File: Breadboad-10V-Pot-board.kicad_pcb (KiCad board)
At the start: 2 copper layers, 50 x 29 mm, 27 parts, among them P1 DIP14, P2 DIP14, U1 TL072-, U2 TL072-, U3 TL072-

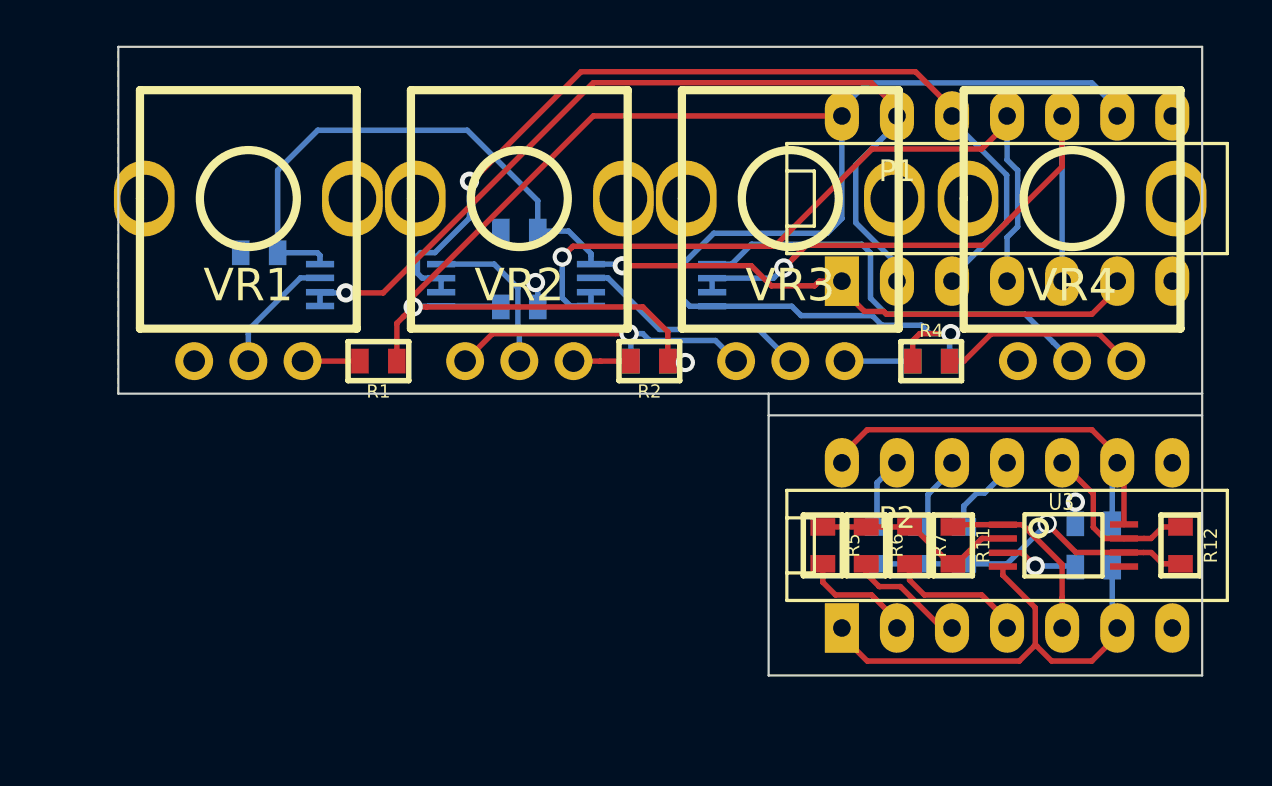
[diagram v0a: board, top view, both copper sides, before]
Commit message: added jack board and laid out mechanical holes for panel separation
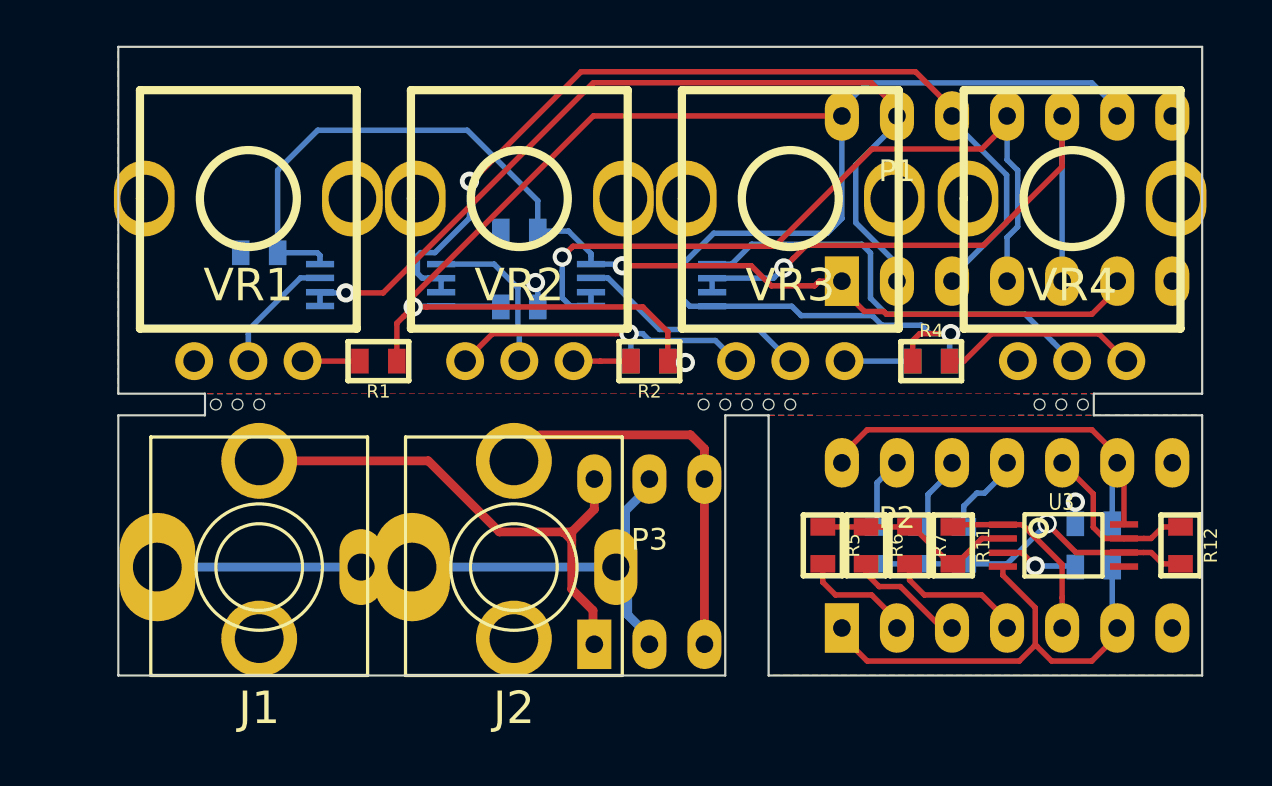
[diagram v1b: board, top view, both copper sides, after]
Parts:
- added HOLE-0.125-INCH: VAL**, MyModules:HOLE-0.125-INCH, F.Cu at (95.5, 48.5)
- added HOLE-0.125-INCH: VAL**, MyModules:HOLE-0.125-INCH, F.Cu at (120.0, 48.5)
- added HOLE-0.125-INCH: VAL**, MyModules:HOLE-0.125-INCH, F.Cu at (96.5, 48.5)
- added HOLE-0.125-INCH: VAL**, MyModules:HOLE-0.125-INCH, F.Cu at (107.8, 48.5)
- added HOLE-0.125-INCH: VAL**, MyModules:HOLE-0.125-INCH, F.Cu at (127.8, 48.5)
- added HOLE-0.125-INCH: VAL**, MyModules:HOLE-0.125-INCH, F.Cu at (97.5, 48.5)
- added HOLE-0.125-INCH: VAL**, MyModules:HOLE-0.125-INCH, F.Cu at (119.0, 48.5)
- added HOLE-0.125-INCH: VAL**, MyModules:HOLE-0.125-INCH, F.Cu at (118.0, 48.5)
- added HOLE-0.125-INCH: VAL**, MyModules:HOLE-0.125-INCH, F.Cu at (122.0, 48.5)
- added HOLE-0.125-INCH: VAL**, MyModules:HOLE-0.125-INCH, F.Cu at (133.5, 48.5)
- added HOLE-0.125-INCH: VAL**, MyModules:HOLE-0.125-INCH, F.Cu at (134.5, 48.5)
- added HOLE-0.125-INCH: VAL**, MyModules:HOLE-0.125-INCH, F.Cu at (121.0, 48.5)
- added HOLE-0.125-INCH: VAL**, MyModules:HOLE-0.125-INCH, F.Cu at (135.5, 48.5)
- added J1: JACK_MONO_SW, MyModules:PJ-301B-JACK, F.Cu at (97.5, 56.0)
- added J2: JACK_MONO_SW, MyModules:PJ-301B-JACK, F.Cu at (109.2, 56.0)
- added P3: DIP_6, Housings_DIP:DIP-6__300_ELL, F.Cu at (115.5, 55.8)
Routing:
- net GND: track 20.6 -> 50.7 mm
- net JACK1: track 0.00 -> 24.9 mm
- net JACK2: track 0.00 -> 18.6 mm
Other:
- outline, holes or cut-outs redrawn
- rule trace_min: 0.254 -> 0.2032

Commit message: cleaning up silkscreen
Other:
- board text added: "+"
- board text added: "+V"
- board text added: "-"
- board text added: "1"
- board text added: "12V+"
- board text added: "2"
- board text added: "3"
- board text added: "4"
- board text added: "A1"
- board text added: "A2"
- board text added: "A3"
- board text added: "AOUT"
- board text added: "B1"
- board text added: "B2"
- board text added: "B3"
- board text added: "BOUT"
- board text added: "CV BUDDY 0-10V"
- board text added: "GND"
- board text added: "V"

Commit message: silkscreen adjusted, ready to order. May have problem with NPTH holes with DirtyPCBs
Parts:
- added P3: DIP_6, Housings_DIP:DIP-6__300_ELL, F.Cu at (102.9, 55.9)
- moved P3 0.15 mm to (115.6, 55.9)
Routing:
- net JACK1: track 24.9 -> 10.9 mm
- net GND: track 50.7 -> 52.9 mm
- net JACK2: track 18.6 -> 20.3 mm
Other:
- board text added: "A"
- board text added: "B"
- board text added: "CV BUD 0-10V"
- board text added: "JACK BUD"
- board text added: "MIX BUD"
- board text added: "OUT"
- board text added: "V+"
- board text added: "V-"
- board text removed: "+V"
- board text removed: "AOUT"
- board text removed: "BOUT"
- board text removed: "CV BUDDY 0-10V"
- board text removed: "V"

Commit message: sent for fabrication
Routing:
- net GND: track 52.9 -> 135.1 mm
